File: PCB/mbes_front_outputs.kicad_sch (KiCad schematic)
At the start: 55 parts, among them Q1 BC817, Q11 TPCA8120,L1Q, Q14 BC817, Q15 BC817, Q19 BC817, Q2 BC817, Q20 BC817, Q21 BC817, Q3 BC817, Q4 TPCA8120,L1Q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

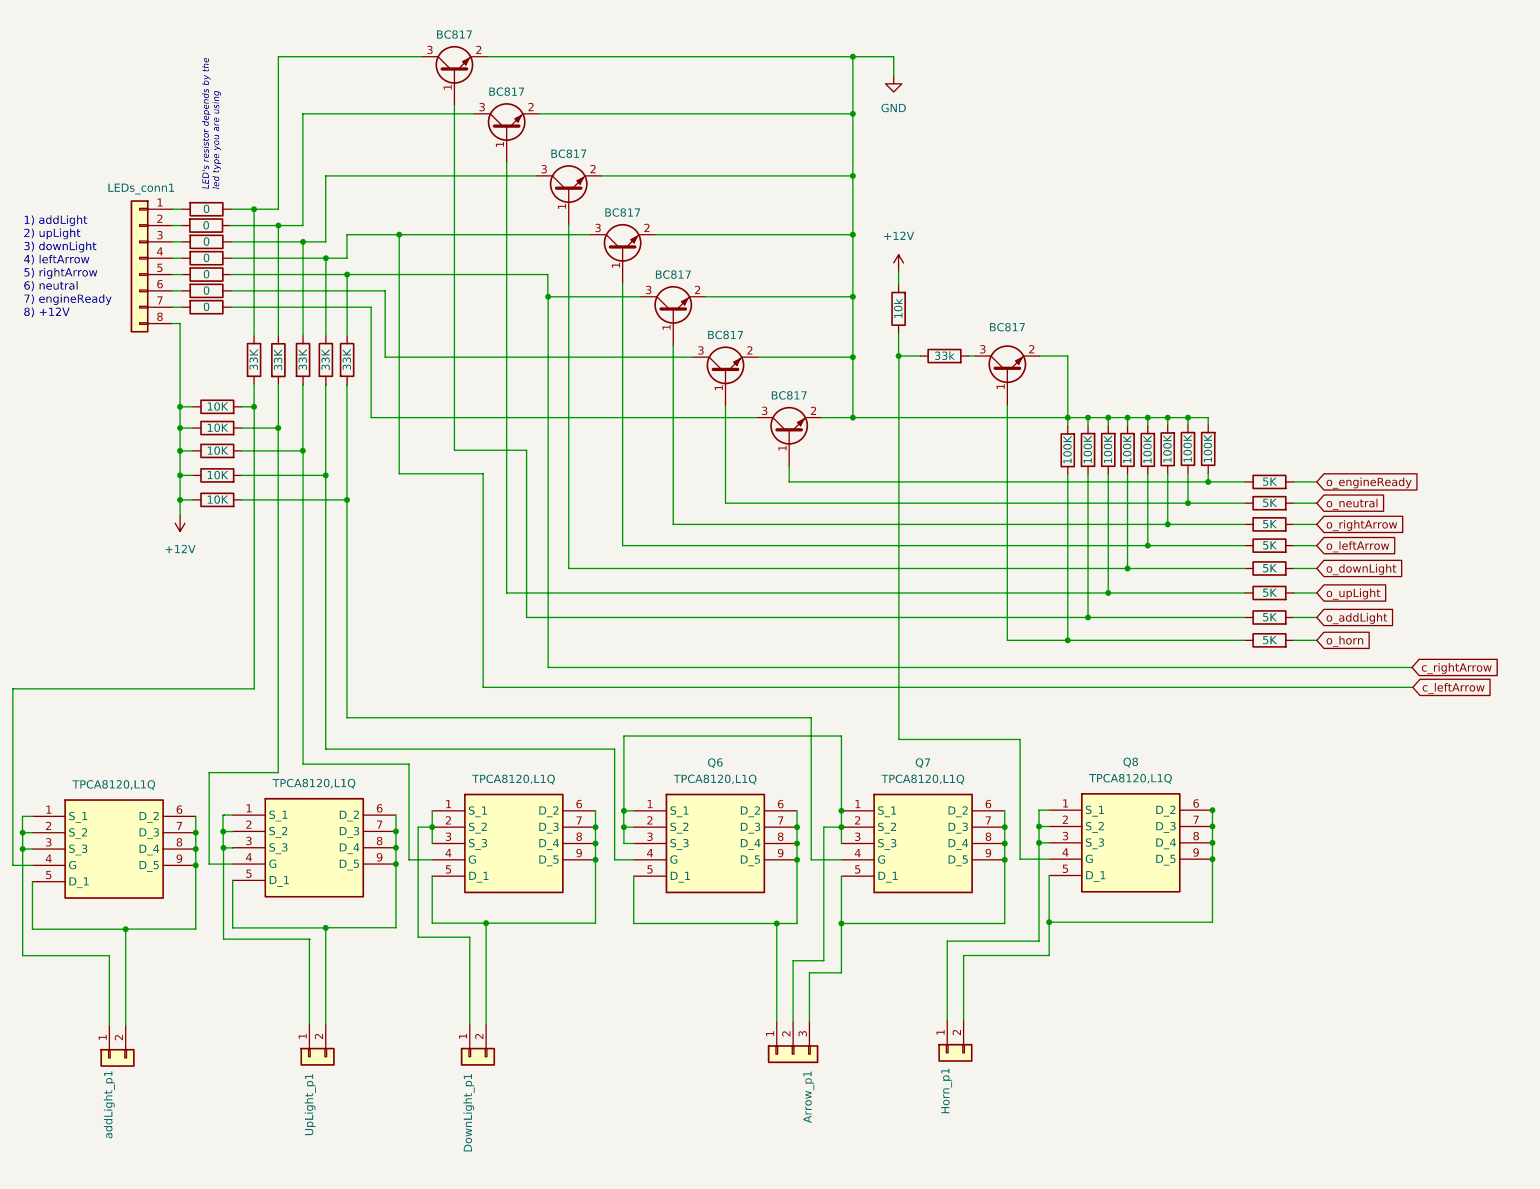
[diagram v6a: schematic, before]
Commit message: o_NEUTRAL is connected directly to the led
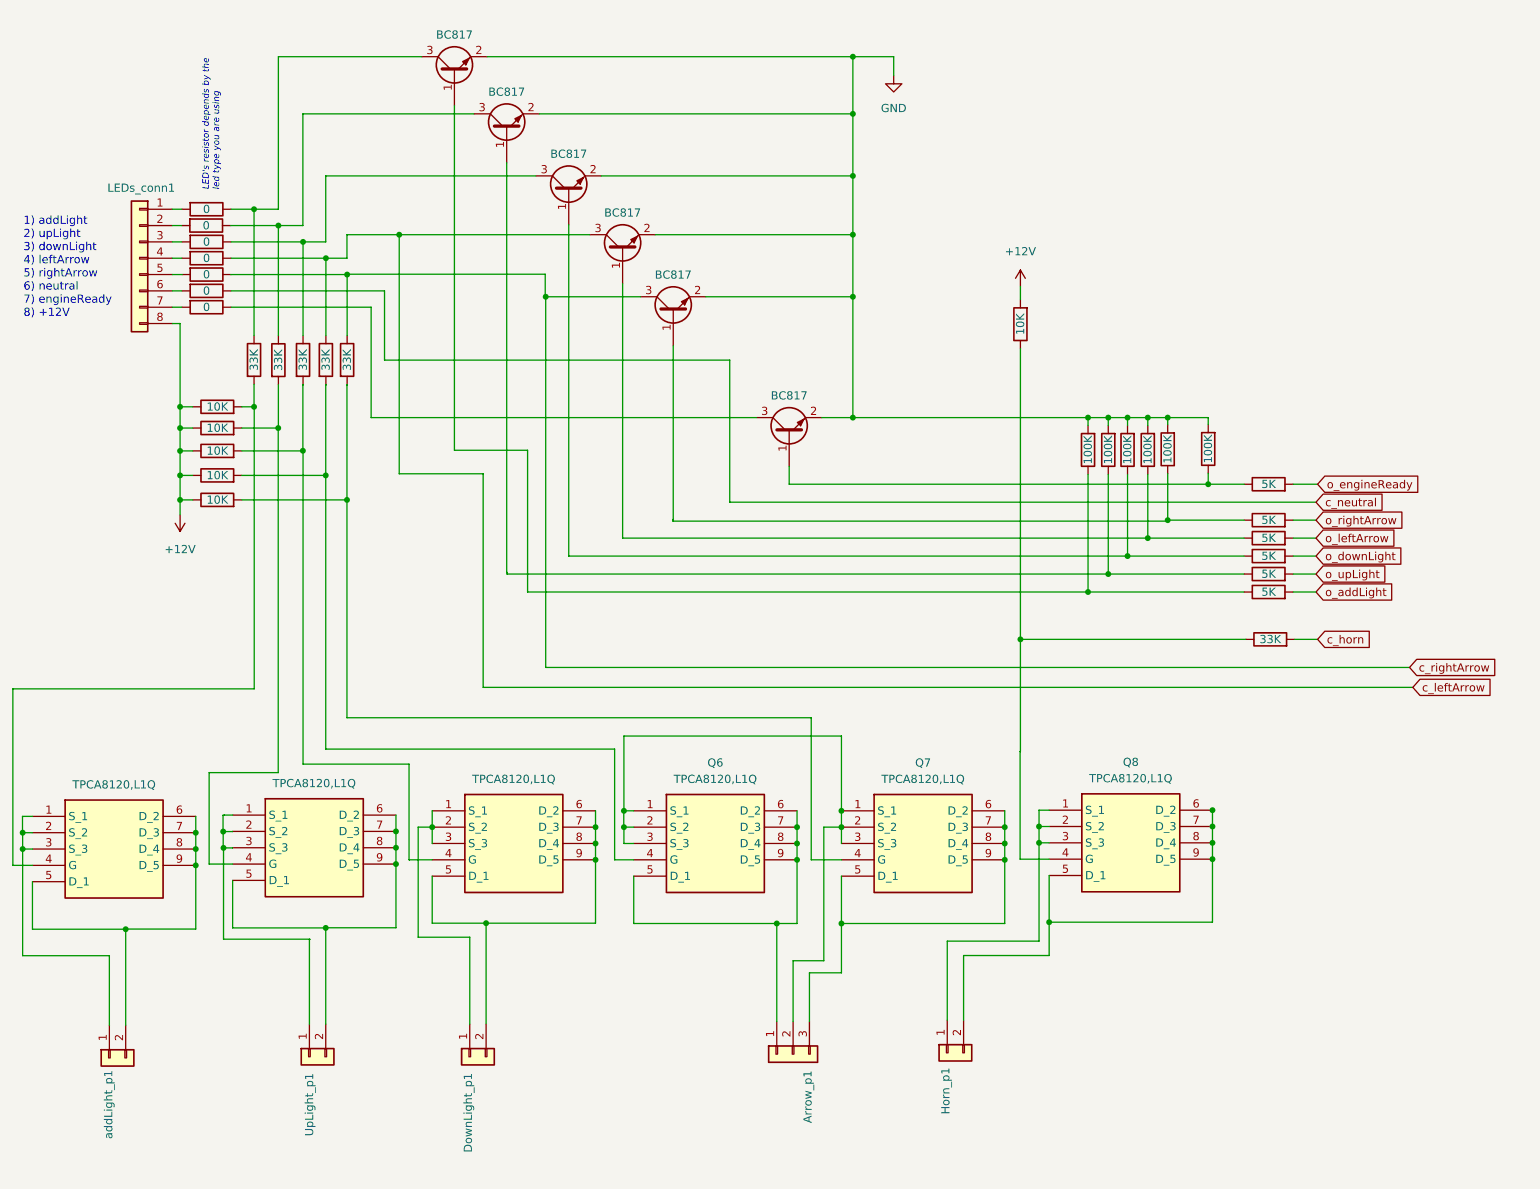
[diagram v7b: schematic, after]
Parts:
- removed Q20, Q3: BC817, Package_TO_SOT_SMD:SOT-23, symbol Transistor_BJT:BC817
- removed RA15: 33k, Resistor_SMD:R_1206_3216Metric, symbol Device:R
- removed RA17: 5K, Resistor_SMD:R_1206_3216Metric, symbol Device:R
- removed RA32, RA39: 100K, Resistor_SMD:R_1206_3216Metric, symbol Device:R
- RA42: value 10k -> 10K
- RA7: value 5K -> 33K
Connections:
- net at RA7.1: now also Q8.4 (G), RA42.1
- net c_neutral: now reaches RA6.1
- net o_horn renamed c_horn

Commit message: No USB support and PCB-B size reducing
Implementing USB power support using 7805 was a stupid idea: too much wasted electic current in Joule effect. So, I moved just
one 7805 in the PCB-A, because the its used power is very low. It allowed me to optimize the PCB-B used space and reduce its
whole size ;-)
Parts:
- LEDs_conn1: footprint Connector_PinHeader_2.54mm:PinHeader_1x08_P2.54mm_Vertical -> Connector_PinHeader_2.54mm:PinHeader_2x04_P2.54mm_Vertical
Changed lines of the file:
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@@
 			)
 		)
-		(property "Footprint" "Connector_PinHeader_2.54mm:PinHeader_1x08_P2.54mm_Vertical"
+		(property "Footprint" "Connector_PinHeader_2.54mm:PinHeader_2x04_P2.54mm_Vertical"
 			(at 35.2044 51.9684 0)
 			(effects
